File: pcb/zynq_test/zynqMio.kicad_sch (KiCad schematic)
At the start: 31 parts, among them SW201 SW_SPDT, SW202 SW_SPDT, SW203 SW_SPDT, U201 DSC1001CI2-033.3300, U202 XC7Z020-2CLG400I

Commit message: Finished Power Supply
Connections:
- net +3.3V renamed +3V3
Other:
- title: (none) -> Zynq PS IO
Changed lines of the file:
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@@
 	(paper "A4")
 	(title_block
-		(date "2025-09-06")
-		(rev "v1.0")
+		(title "Zynq PS IO")
+		(date "2025-09-13")
+		(rev "A")
 	)
 	(bus_alias "ETH"
@@
 	(wire
 		(pts
-			(xy 88.9 114.3) (xy 93.98 114.3)
+			(xy 85.09 114.3) (xy 93.98 114.3)
 		)
 		(stroke
@@
 	)
 	(label "MODE-5"
-		(at 88.9 114.3 180)
+		(at 85.09 114.3 0)
 		(effects
 			(font
 				(size 1.27 1.27)
 			)
-			(justify right bottom)
+			(justify left bottom)
 		)
 	)
@@
 			)
 		)
-		(property "Value" "+3.3V"
+		(property "Value" "+3V3"
 			(at 117.094 113.03 0)
 			(effects
@@
 			)
 		)
-		(property "Value" "+3.3V"
+		(property "Value" "+3V3"
 			(at 109.728 139.954 0)
 			(effects
@@
 			)
 		)
-		(property "Value" "+3.3V"
+		(property "Value" "+3V3"
 			(at 21.59 31.75 0)
 			(effects
@@
 			)
 		)
-		(property "Value" "+3.3V"
+		(property "Value" "+3V3"
 			(at 109.728 176.784 0)
 			(effects
@@
 			)
 		)
-		(property "Value" "+3.3V"
+		(property "Value" "+3V3"
 			(at 21.59 114.3 0)
 			(effects
@@
 			)
 		)
-		(property "Value" "+3.3V"
+		(property "Value" "+3V3"
 			(at 109.728 157.734 0)
 			(effects

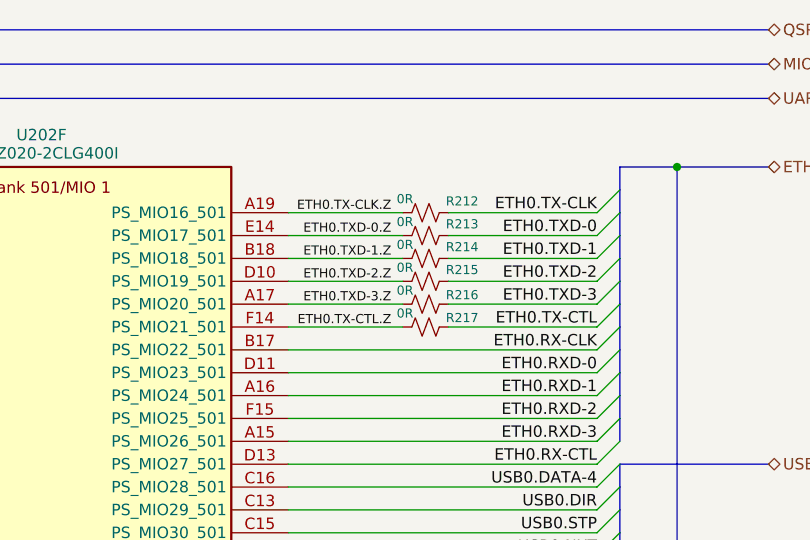
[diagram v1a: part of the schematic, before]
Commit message: Finished most of the schematic, will start routing soon
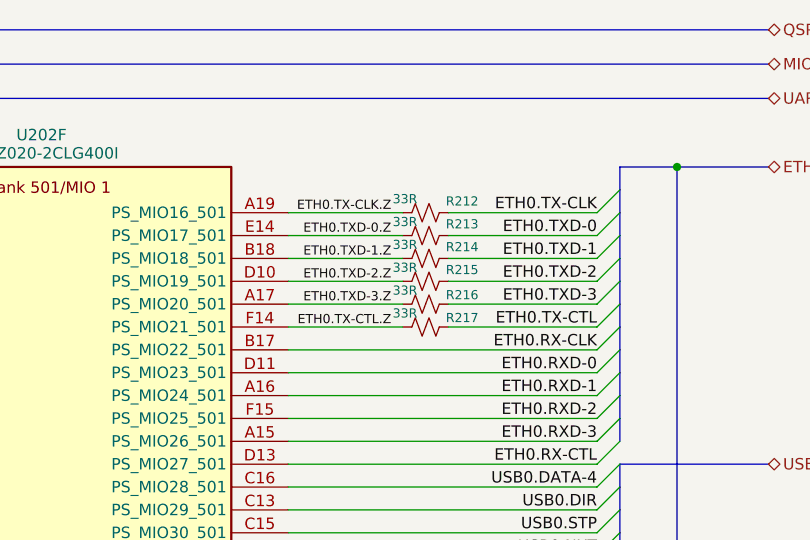
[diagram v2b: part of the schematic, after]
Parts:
- R212, R213, R214, R215, R216, R217: value 0R -> 33R
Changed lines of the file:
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@@
 			)
 		)
-		(property "Value" "0R"
+		(property "Value" "33R"
 			(at 226.314 44.196 90)
 			(effects
@@
 			)
 		)
-		(property "Value" "0R"
+		(property "Value" "33R"
 			(at 226.314 49.276 90)
 			(effects
@@
 			)
 		)
-		(property "Value" "0R"
+		(property "Value" "33R"
 			(at 226.314 41.656 90)
 			(effects
@@
 			)
 		)
-		(property "Value" "0R"
+		(property "Value" "33R"
 			(at 226.314 46.736 90)
 			(effects
@@
 			)
 		)
-		(property "Value" "0R"
+		(property "Value" "33R"
 			(at 226.314 39.116 90)
 			(effects
@@
 			)
 		)
-		(property "Value" "0R"
+		(property "Value" "33R"
 			(at 226.314 51.816 90)
 			(effects

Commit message: Finished to first ddr ic
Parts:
- U202: footprint Package_BGA:Xilinx_CLG400 -> Zynq:Zynq_Z7020-2CLG400I_W_Delay
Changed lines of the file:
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@@
 			)
 		)
-		(property "Footprint" "Package_BGA:Xilinx_CLG400"
+		(property "Footprint" "Zynq:Zynq_Z7020-2CLG400I_W_Delay"
 			(at 34.29 -16.51 0)
 			(effects
@@
 			)
 		)
-		(property "Footprint" "Package_BGA:Xilinx_CLG400"
+		(property "Footprint" "Zynq:Zynq_Z7020-2CLG400I_W_Delay"
 			(at 157.48 13.97 0)
 			(effects

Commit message: finished diff of HDMI
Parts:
- C201, C205: footprint (none) -> Capacitor_SMD:C_1210_3225Metric
- C203, C204, C206, C207, C208: footprint (none) -> Capacitor_SMD:C_0402_1005Metric
- R202, R203, R204, R205, R206, R207, R208, R209, R212, R213, R214, R215, R216, R217, R218: footprint (none) -> Resistor_SMD:R_0402_1005Metric
- R210, R211: footprint (none) -> Resistor_SMD:R_0201_0603Metric
- U201: footprint (none) -> other:DSC1001
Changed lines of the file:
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@@
 			)
 		)
-		(property "Footprint" ""
+		(property "Footprint" "Resistor_SMD:R_0402_1005Metric"
 			(at 91.694 145.034 90)
 			(effects
@@
 			)
 		)
-		(property "Footprint" ""
+		(property "Footprint" "Capacitor_SMD:C_0402_1005Metric"
 			(at 37.7952 50.8 0)
 			(effects
@@
 			)
 		)
-		(property "Footprint" ""
+		(property "Footprint" "Resistor_SMD:R_0402_1005Metric"
 			(at 228.6 45.72 0)
 			(effects
@@
 			)
 		)
-		(property "Footprint" ""
+		(property "Footprint" "Resistor_SMD:R_0402_1005Metric"
 			(at 114.046 119.634 90)
 			(effects
@@
 			)
 		)
-		(property "Footprint" ""
+		(property "Footprint" "Resistor_SMD:R_0402_1005Metric"
 			(at 91.694 181.864 90)
 			(effects
@@
 			)
 		)
-		(property "Footprint" ""
+		(property "Footprint" "Resistor_SMD:R_0201_0603Metric"
 			(at 149.606 80.264 90)
 			(effects
@@
 			)
 		)
-		(property "Footprint" ""
+		(property "Footprint" "Resistor_SMD:R_0201_0603Metric"
 			(at 149.606 90.424 90)
 			(effects
@@
 			)
 		)
-		(property "Footprint" ""
+		(property "Footprint" "Capacitor_SMD:C_0402_1005Metric"
 			(at 159.7152 93.98 0)
 			(effects
@@
 			)
 		)
-		(property "Footprint" ""
+		(property "Footprint" "Resistor_SMD:R_0402_1005Metric"
 			(at 134.874 119.126 90)
 			(effects
@@
 			)
 		)
-		(property "Footprint" ""
+		(property "Footprint" "Resistor_SMD:R_0402_1005Metric"
 			(at 228.6 50.8 0)
 			(effects
@@
 			)
 		)
-		(property "Footprint" ""
+		(property "Footprint" "Capacitor_SMD:C_1210_3225Metric"
 			(at 138.1252 49.53 0)
 			(effects
@@
 			)
 		)
-		(property "Footprint" ""
+		(property "Footprint" "Resistor_SMD:R_0402_1005Metric"
 			(at 228.6 43.18 0)
 			(effects
@@
 			)
 		)
-		(property "Footprint" ""
+		(property "Footprint" "Capacitor_SMD:C_0402_1005Metric"
 			(at 145.7452 49.53 0)
 			(effects
@@
 			)
 		)
-		(property "Footprint" ""
+		(property "Footprint" "Resistor_SMD:R_0402_1005Metric"
 			(at 91.694 162.814 90)
 			(effects
@@
 			)
 		)
-		(property "Footprint" ""
+		(property "Footprint" "Resistor_SMD:R_0402_1005Metric"
 			(at 94.996 119.634 90)
 			(effects
@@
 			)
 		)
-		(property "Footprint" ""
+		(property "Footprint" "Capacitor_SMD:C_1210_3225Metric"
 			(at 22.5552 50.8 0)
 			(effects
@@
 			)
 		)
-		(property "Footprint" ""
+		(property "Footprint" "Resistor_SMD:R_0402_1005Metric"
 			(at 228.6 48.26 0)
 			(effects
@@
 			)
 		)
-		(property "Footprint" ""
+		(property "Footprint" "Resistor_SMD:R_0402_1005Metric"
 			(at 136.144 147.066 90)
 			(effects
@@
 			)
 		)
-		(property "Footprint" ""
+		(property "Footprint" "Resistor_SMD:R_0402_1005Metric"
 			(at 228.6 40.64 0)
 			(effects
@@
 			)
 		)
-		(property "Footprint" ""
+		(property "Footprint" "Resistor_SMD:R_0402_1005Metric"
 			(at 228.6 53.34 0)
 			(effects
@@
 			)
 		)
-		(property "Footprint" ""
+		(property "Footprint" "Capacitor_SMD:C_0402_1005Metric"
 			(at 30.1752 50.8 0)
 			(effects
@@
 			)
 		)
-		(property "Footprint" ""
+		(property "Footprint" "Capacitor_SMD:C_0402_1005Metric"
 			(at 153.3652 49.53 0)
 			(effects
@@
 			)
 		)
-		(property "Footprint" ""
+		(property "Footprint" "other:DSC1001"
 			(at 38.1 127 0)
 			(effects
@@
 			)
 		)
-		(property "Footprint" ""
+		(property "Footprint" "Resistor_SMD:R_0402_1005Metric"
 			(at 101.6 55.88 0)
 			(effects
@@
 			)
 		)
-		(property "Footprint" ""
+		(property "Footprint" "Resistor_SMD:R_0402_1005Metric"
 			(at 229.87 101.6 0)
 			(effects

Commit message: Almost done with BOM
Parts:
- removed SW201, SW202, SW203: SW_SPDT, symbol Switch:SW_SPDT
- added R219, R220, R221: 1k, Resistor_SMD:R_0402_1005Metric, symbol Device:R_US
- added SW201: SW_DIP_x03, Button_Switch_SMD:SW_DIP_SPSTx03_Slide_6.7x9.18mm_W8.61mm_P2.54mm_LowProfile, symbol Switch:SW_DIP_x03
- C202: footprint (none) -> Capacitor_SMD:C_0402_1005Metric
- R201: footprint (none) -> Resistor_SMD:R_0402_1005Metric
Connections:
- net +3V3: now also R219.2, R220.2, R221.2
- net GND: now also SW201.4, SW201.5, SW201.6
- net at R202.2: now also R219.1, SW201.1
- net at R204.2: now also R221.1, SW201.3
- net at R203.2: now also R220.1, SW201.2
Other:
- moved on the sheet: R202, R203, R204

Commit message: Version sent to JLCPCB
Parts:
- C201, C205: JLCPCB Part# (none) -> C23742; PART_NUMBER (none) -> CL32A107MPVNNNE
- C202: JLCPCB Part# (none) -> C1525; PART_NUMBER (none) -> CL05B104KO5NNNC
- C203, C206: JLCPCB Part# (none) -> C23733; PART_NUMBER (none) -> CL05A475MP5NRNC
- C204, C207: JLCPCB Part# (none) -> C88946; PART_NUMBER (none) -> GRM155R71A474KE01D
- C208: JLCPCB Part# (none) -> C77013; PART_NUMBER (none) -> GRM155R71E103KA01D
- R201, R206, R218: JLCPCB Part# (none) -> C242160; PART_NUMBER (none) -> ERJ2GE0R00X
- R202, R203, R204, R205, R207, R208, R209: JLCPCB Part# (none) -> C409859; PART_NUMBER (none) -> ERJ2GEJ203X
- R210, R211: JLCPCB Part# (none) -> C102684; PART_NUMBER (none) -> RTT011002FTH
- R212, R213, R214, R215, R216, R217: JLCPCB Part# (none) -> C264051; PART_NUMBER (none) -> ERJ2GEJ330X
- R219, R220, R221: JLCPCB Part# (none) -> C242161; PART_NUMBER (none) -> ERJ2RKF1001X
- SW201: JLCPCB Part# (none) -> C6533469; PART_NUMBER (none) -> CFS-0301MB
- U201: JLCPCB Part# (none) -> C611402; PART_NUMBER (none) -> DSC1001CI2-033.3300
- U202: JLCPCB Part# (none) -> C569043; PART_NUMBER (none) -> XC7Z020-2CLG400I
